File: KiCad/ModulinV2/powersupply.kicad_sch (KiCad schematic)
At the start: 35 parts, among them IC27 NCP5500DADJR2G, IC28 NCP5500DADJR2G, IC29 NCP5500DADJR2G, IC30 NCP5500DADJR2G, IC31 LM2576S-12_NOPB, IC32 LM2576S-12_NOPB, J4 PJ-002B

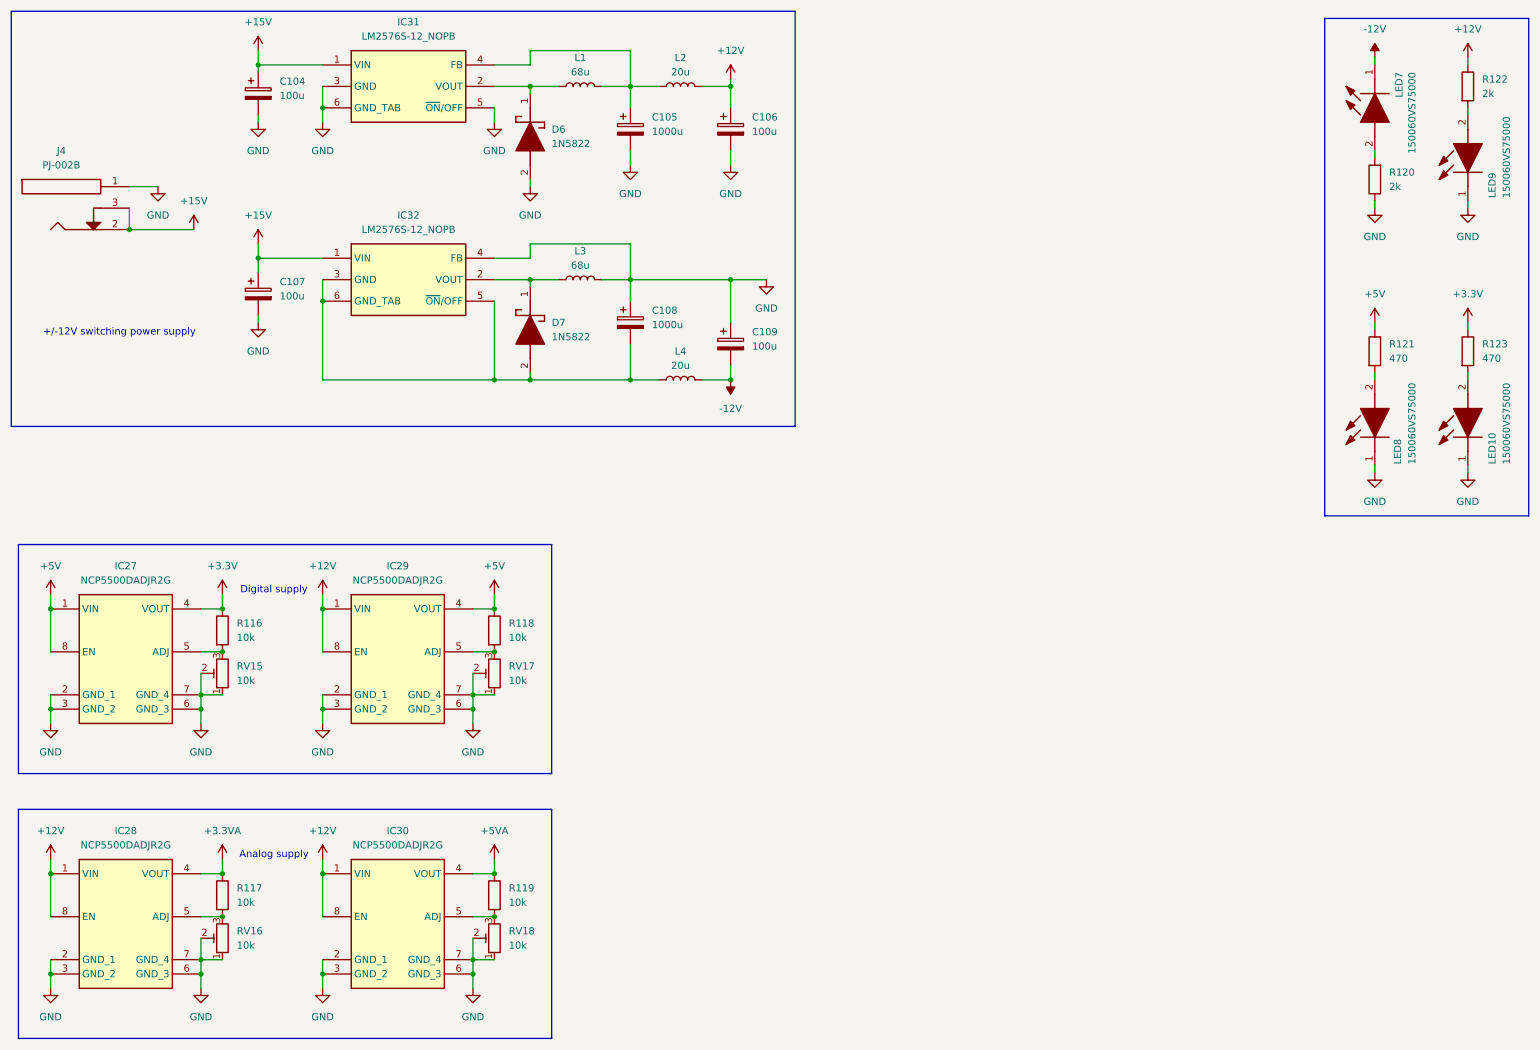
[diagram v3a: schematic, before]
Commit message: Added wave selection jumpers for testing
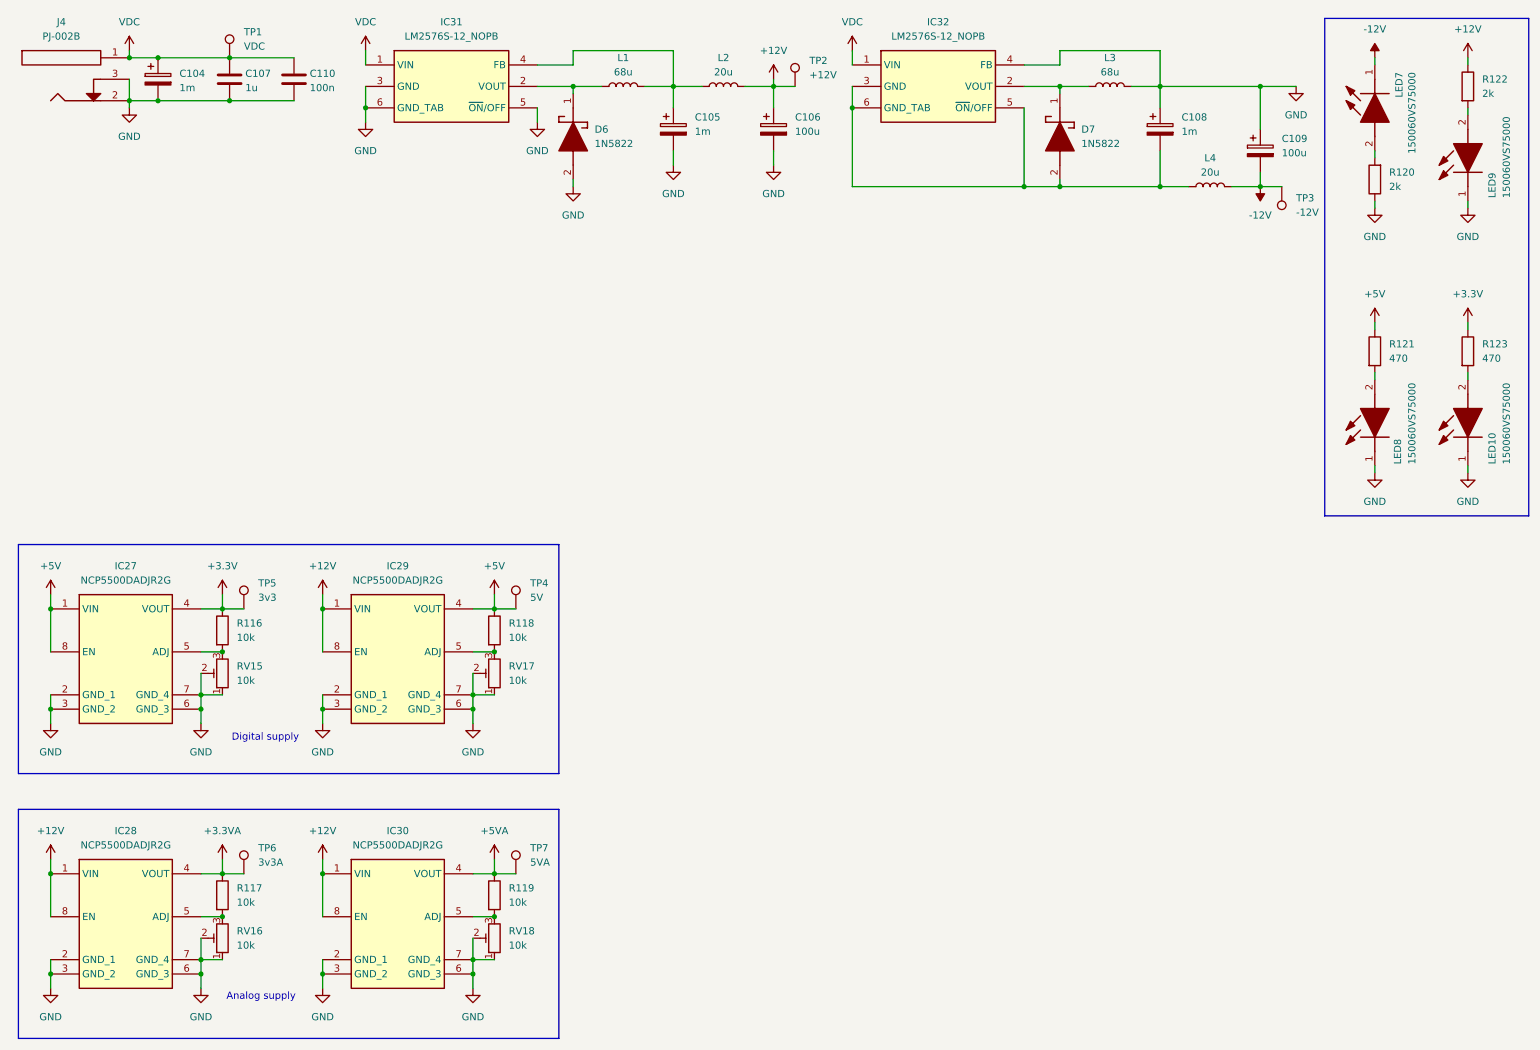
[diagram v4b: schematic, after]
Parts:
- removed C107: 100u, symbol Device:C_Polarized
- added C107: 1u, symbol Device:C
- added C110: 100n, symbol Device:C
- added TP1: VDC, symbol Connector:TestPoint
- added TP2: +12V, symbol Connector:TestPoint
- added TP3: -12V, symbol Connector:TestPoint
- added TP4: 5V, symbol Connector:TestPoint
- added TP5: 3v3, symbol Connector:TestPoint
- added TP6: 3v3A, symbol Connector:TestPoint
- added TP7: 5VA, symbol Connector:TestPoint
- C104: value 100u -> 1m
- C105, C108: value 1000u -> 1m
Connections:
- net +12V: now also TP2.1
- net +3.3V: now also TP5.1
- net +3.3VA: now also TP6.1
- net +5V: now also TP4.1
- net +5VA: now also TP7.1
- net -12V: now also TP3.1
- net GND: now also J4.2, J4.3, C107.2, C110.2; no longer J4.1
- net +15V renamed VDC
- net VDC: now also J4.1, C107.1, C110.1, TP1.1; no longer J4.2, J4.3
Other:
- note removed: "+/-12V switching power supply"
- moved on the sheet: C104, C105, C106, C108, C109, D6, D7, IC31, IC32, J4, L1, L2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

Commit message: Added L7812 regulators as backup power supply option
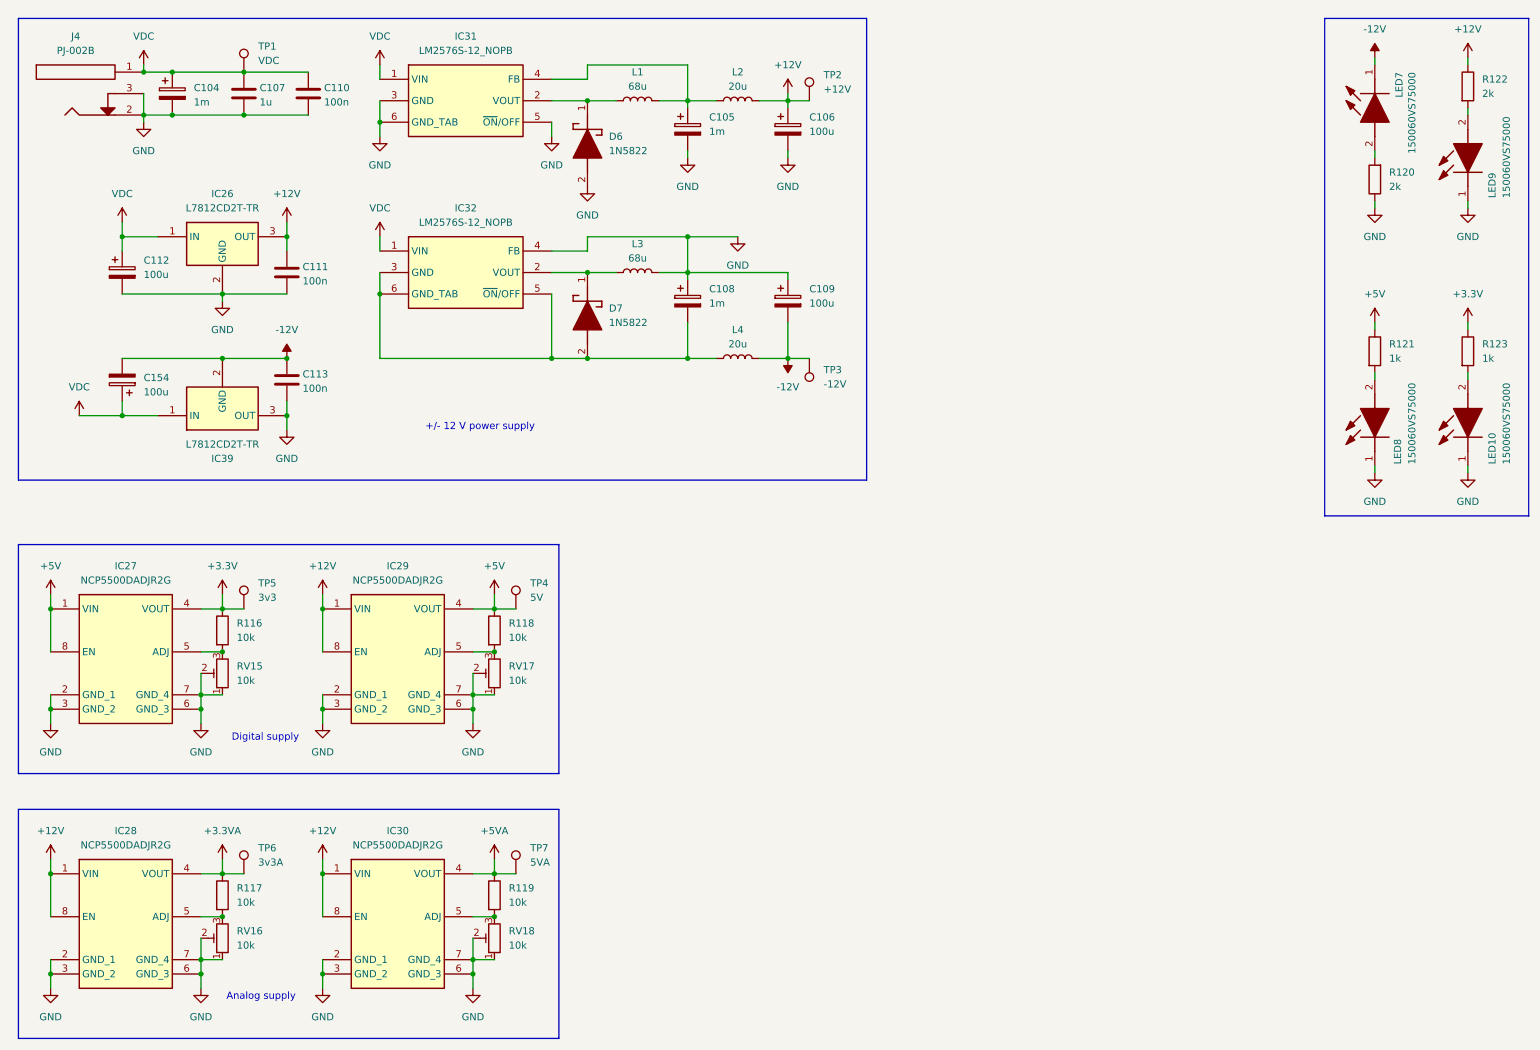
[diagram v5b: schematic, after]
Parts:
- added C111, C113: 100n, symbol Device:C
- added C112, C154: 100u, symbol Device:C_Polarized
- added IC26, IC39: L7812CD2T-TR, L7812CD2TTR, symbol L7812CD2T-TR:L7812CD2T-TR
- R121, R123: value 470 -> 1k
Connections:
- net +12V: now also C111.1, IC26.3 (OUT)
- net -12V: now also C113.1, C154.2, IC39.2 (GND)
- net GND: now also C111.2, C112.2, C113.2, IC26.2 (GND), IC39.3 (OUT)
- net VDC: now also C112.1, C154.1, IC26.1 (IN), IC39.1 (IN)
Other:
- note added: "+/- 12 V power supply"
- moved on the sheet: C104, C105, C106, C107, C108, C109, C110, D6, D7, IC31, IC32, J4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

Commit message: Added fuse and polarity protection to supply schematic
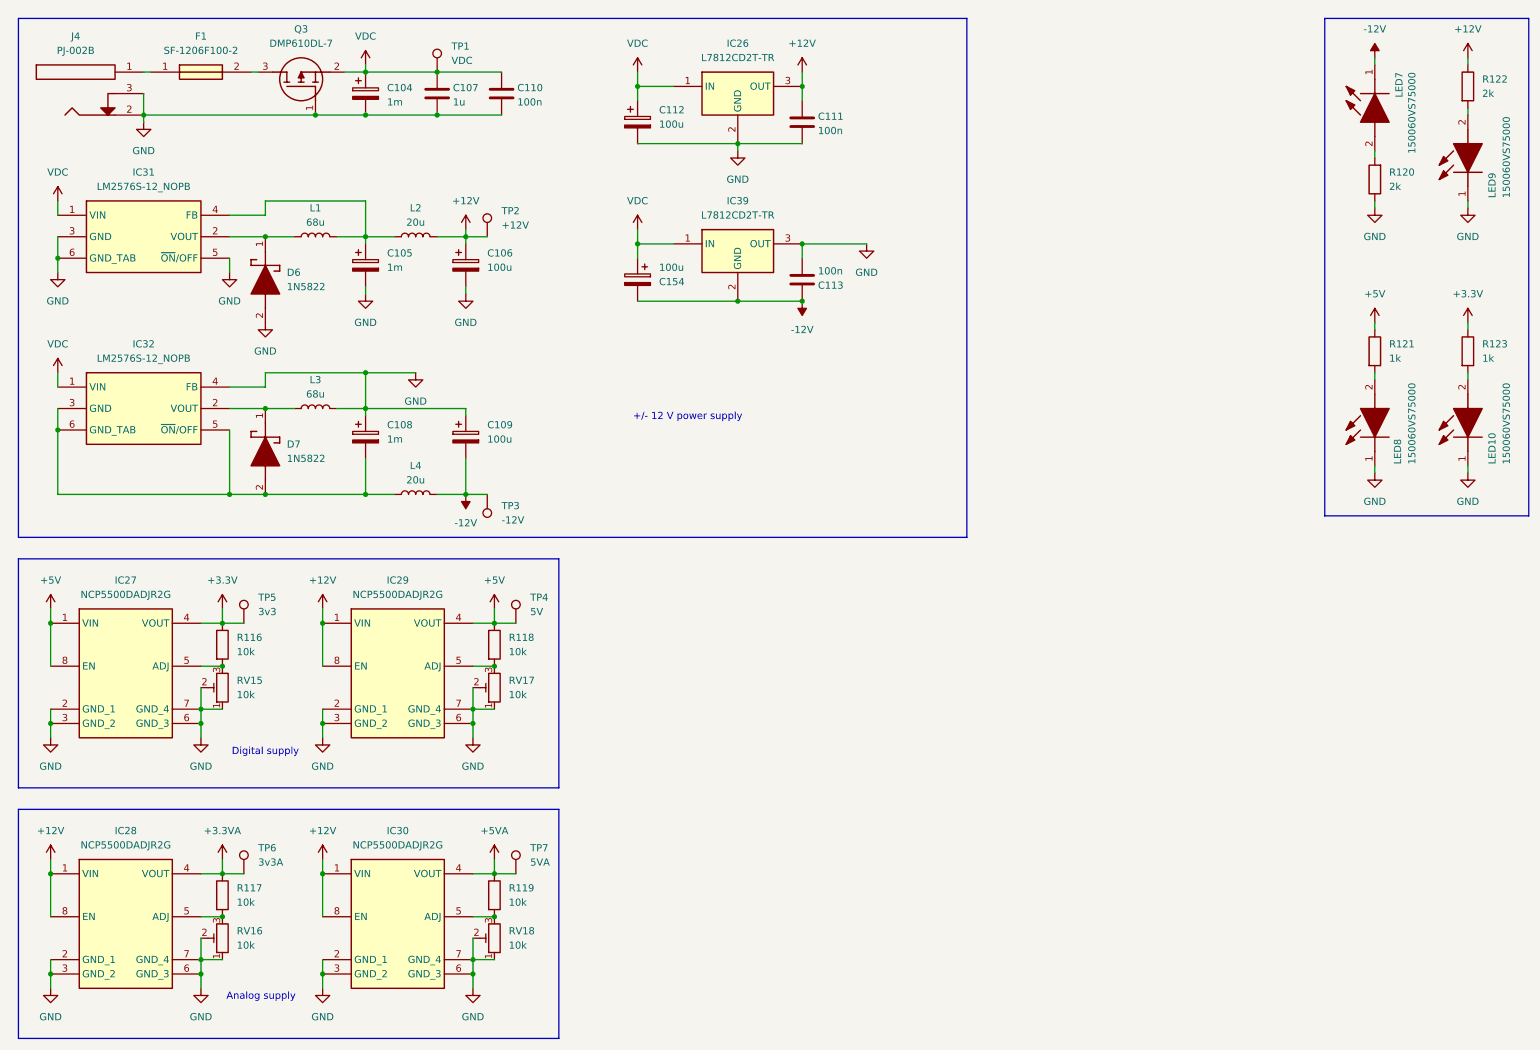
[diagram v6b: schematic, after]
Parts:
- added F1: SF-1206F100-2, FUSC3116X70N, symbol SF-1206F100-2:SF-1206F100-2
- added Q3: DMP610DL-7, SOT96P240X110-3N, symbol DMP610DL-7:DMP610DL-7
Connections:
- net GND: now also Q3.1 (G)
- net VDC: now also Q3.2 (S); no longer J4.1
- new net: F1.1, J4.1
- new net: F1.2, Q3.3 (D)
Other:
- moved on the sheet: C104, C105, C106, C107, C108, C109, C110, C111, C112, C113, C154, D6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

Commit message: Fixed library issues and assigned most footprints
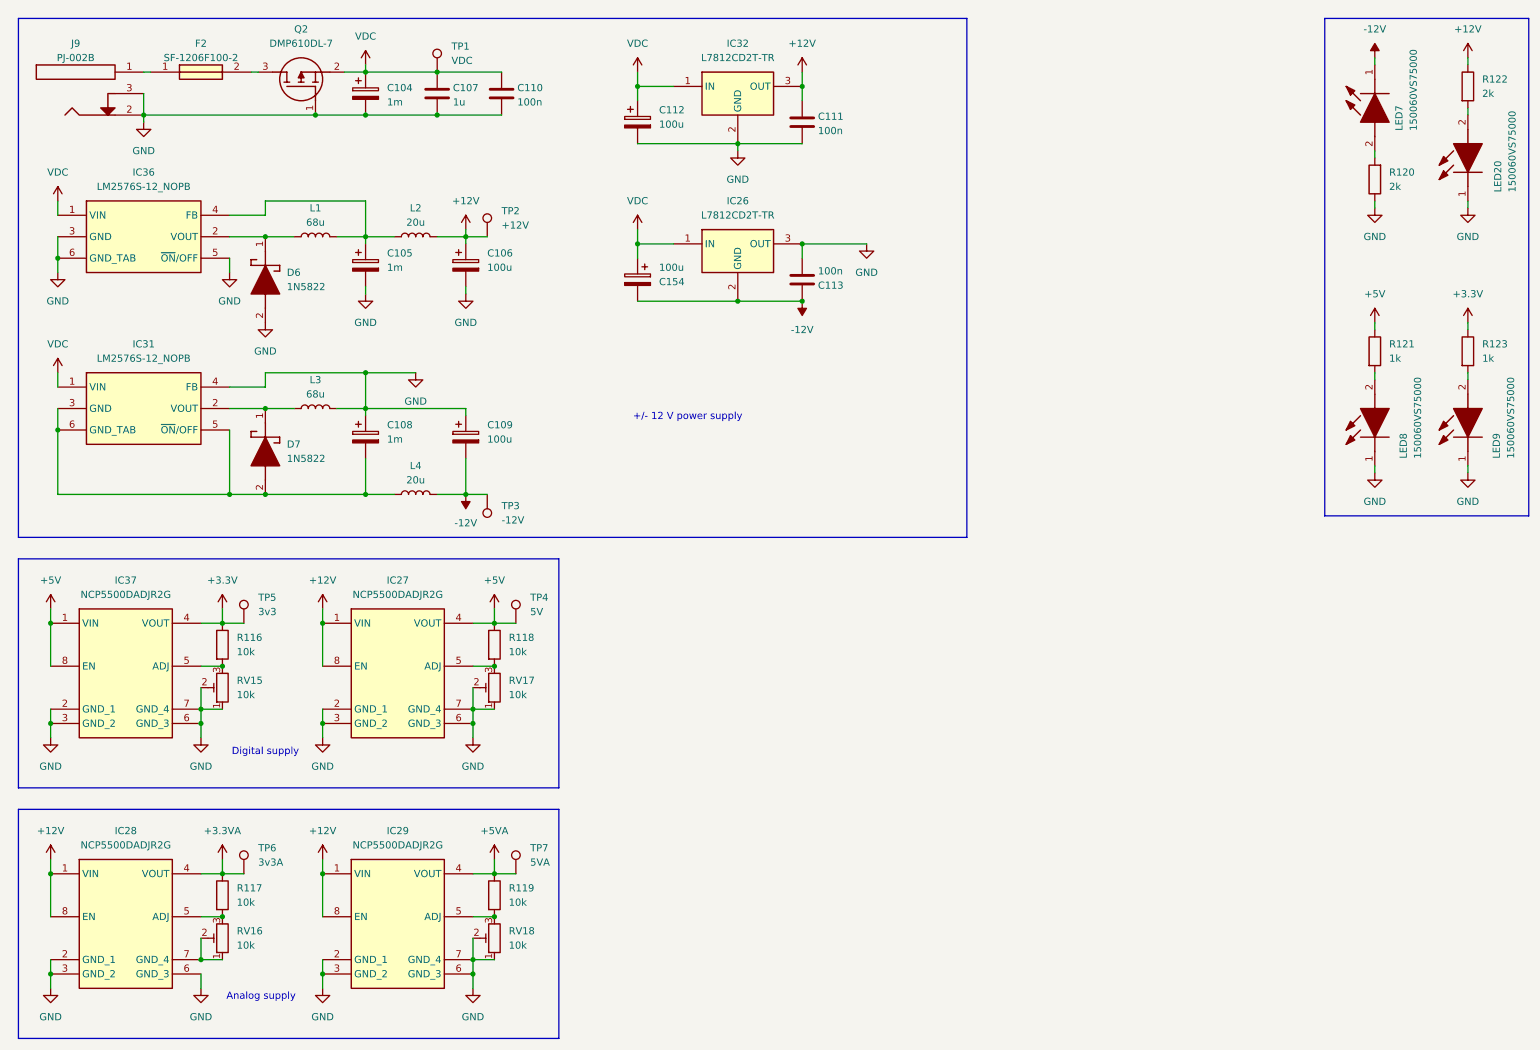
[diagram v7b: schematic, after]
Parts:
- removed F1: SF-1206F100-2, FUSC3116X70N, symbol SF-1206F100-2:SF-1206F100-2
- removed IC26, IC39: L7812CD2T-TR, L7812CD2TTR, symbol L7812CD2T-TR:L7812CD2T-TR
- removed IC27, IC28, IC29, IC30: NCP5500DADJR2G, SOIC127P600X175-8N, symbol NCP5500DADJR2G:NCP5500DADJR2G
- removed IC31, IC32: LM2576S-12_NOPB, TO170P1435X465-6N, symbol LM2576S-12_NOPB:LM2576S-12_NOPB
- removed J4: PJ-002B, PJ002B, symbol PJ-002B:PJ-002B
- removed LED10: 150060VS75000, LEDC1608X80N, symbol 150060VS75000:150060VS75000
- removed Q3: DMP610DL-7, SOT96P240X110-3N, symbol DMP610DL-7:DMP610DL-7
- added F2: SF-1206F100-2, SamacSys_Parts:FUSC3116X70N, symbol SamacSys_Parts:SF-1206F100-2
- added IC26, IC32: L7812CD2T-TR, SamacSys_Parts:L7812CD2TTR, symbol SamacSys_Parts:L7812CD2T-TR
- added IC27, IC28, IC29, IC37: NCP5500DADJR2G, SamacSys_Parts:SOIC127P600X175-8N, symbol SamacSys_Parts:NCP5500DADJR2G
- added IC31, IC36: LM2576S-12_NOPB, SamacSys_Parts:TO170P1435X465-6N, symbol SamacSys_Parts:LM2576S-12_NOPB
- added J9: PJ-002B, SamacSys_Parts:PJ002B, symbol SamacSys_Parts:PJ-002B
- added LED20: 150060VS75000, SamacSys_Parts:LEDC1608X80N, symbol 150060VS75000:150060VS75000
- added Q2: DMP610DL-7, SamacSys_Parts:SOT96P240X110-3N, symbol SamacSys_Parts:DMP610DL-7
- D6, D7: footprint DIOAD3070W130L950D530 -> SamacSys_Parts:DIOAD3070W130L950D530
- LED7, LED8, LED9: footprint LEDC1608X80N -> SamacSys_Parts:LEDC1608X80N
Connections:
- net +12V: now also IC27.1 (VIN), IC27.8 (EN), IC28.1 (VIN), IC28.8 (EN), IC29.1 (VIN), IC29.8 (EN), IC32.3 (OUT)
- net +3.3V: now also IC37.4 (VOUT)
- net +3.3VA: now also IC28.4 (VOUT)
- net +5V: now also IC27.4 (VOUT), IC37.1 (VIN), IC37.8 (EN)
- net +5VA: now also IC29.4 (VOUT)
- net -12V: now also IC26.2 (GND)
- net GND: now also IC26.3 (OUT), IC27.2 (GND_1), IC27.3 (GND_2), IC27.6 (GND_3), IC27.7 (GND_4), IC28.2 (GND_1), IC28.3 (GND_2), IC28.6 (GND_3), IC29.2 (GND_1), IC29.3 (GND_2), IC29.6 (GND_3), IC29.7 (GND_4), IC31.4 (FB), IC32.2 (GND), IC36.3 (GND), IC36.5 (~{ON}/OFF), IC36.6 (GND_TAB), IC37.2 (GND_1), IC37.3 (GND_2), IC37.6 (GND_3), IC37.7 (GND_4), J9.2, J9.3, LED20.1 (K), Q2.1 (G); no longer RV16.1, RV16.2
- net VDC: now also IC26.1 (IN), IC31.1 (VIN), IC32.1 (IN), IC36.1 (VIN), Q2.2 (S)
- net at D7.1 (K), L3.1: now also IC31.2 (VOUT)
- net at C108.2, D7.2 (A), L4.1: now also IC31.3 (GND), IC31.5 (~{ON}/OFF), IC31.6 (GND_TAB)
- net at R119.2, RV18.3: now also IC29.5 (ADJ)
- net at R118.2, RV17.3: now also IC27.5 (ADJ)
- net at R123.2: now also LED9.2 (A)
- net at C105.1, L1.2, L2.1: now also IC36.4 (FB)
- net at R116.2, RV15.3: now also IC37.5 (ADJ)
- net at R122.2: now also LED20.2 (A); no longer LED9.2 (A)
- net at D6.1 (K), L1.1: now also IC36.2 (VOUT)
- net at R117.2, RV16.3: now also IC28.5 (ADJ)
- new net: IC28.7 (GND_4), RV16.1, RV16.2
- new net: F2.1, J9.1
- new net: F2.2, Q2.3 (D)
